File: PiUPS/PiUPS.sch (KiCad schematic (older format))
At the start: 93 parts, among them J1 USB_C_Receptacle_USB2.0, J2 Raspberry_Pi_2_3, J3 USB_A, J4 USB_B_Micro, J5 Screw_Terminal_01x02, J6 Screw_Terminal_01x02, Q1 IRF7404, Q2 IRF7404, Q3 IRLML2803TRPBF, Q4 IRF7404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

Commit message: Updated to include the boges to rev 0.2
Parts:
- removed C8: 100nF, Capacitor_SMD:C_0805_2012Metric_Pad1.18x1.45mm_HandSolder, symbol Device:C
- R14: value 470 -> 100
- R8: value 10k -> 1k
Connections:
- no-connect marks 33 -> 36
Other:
- note added: "(200k)\n\n"
- note added: "(62k)"
- note added: "Ports and outputs + RTC"
- note removed: "Ports and outputs"
- moved on the sheet: BT1, C1, C10, C11, C12, C13, C14, C15, C16, C17, C18, C19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

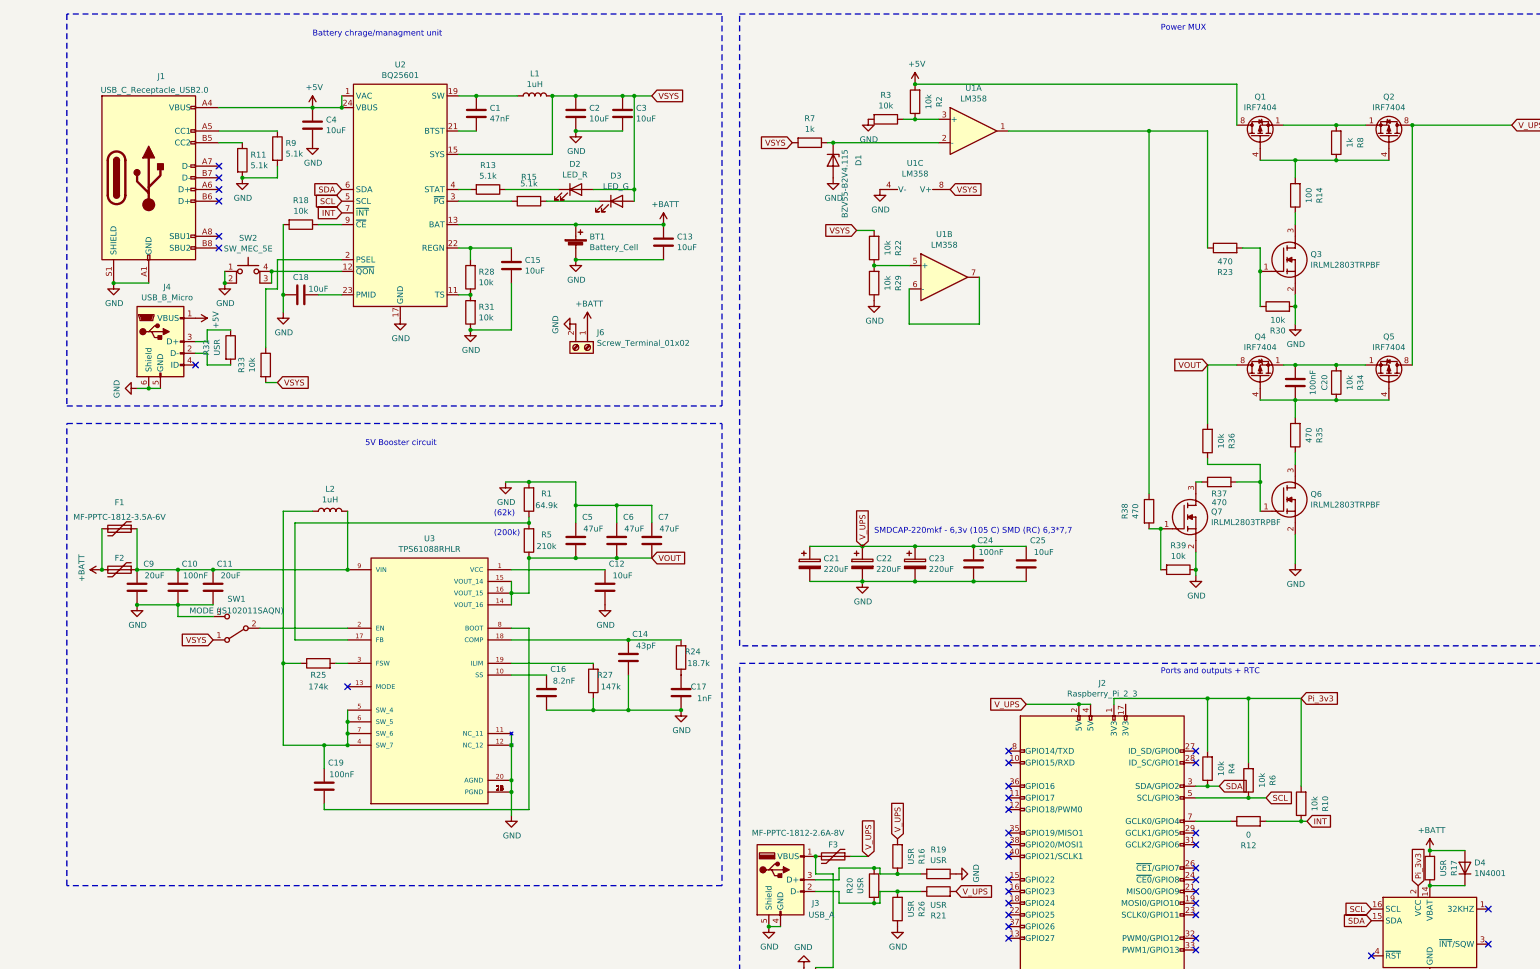
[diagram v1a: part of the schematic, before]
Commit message: added exprimental latching boost IC cutoff circuit + notes about dev branch file and future things to do
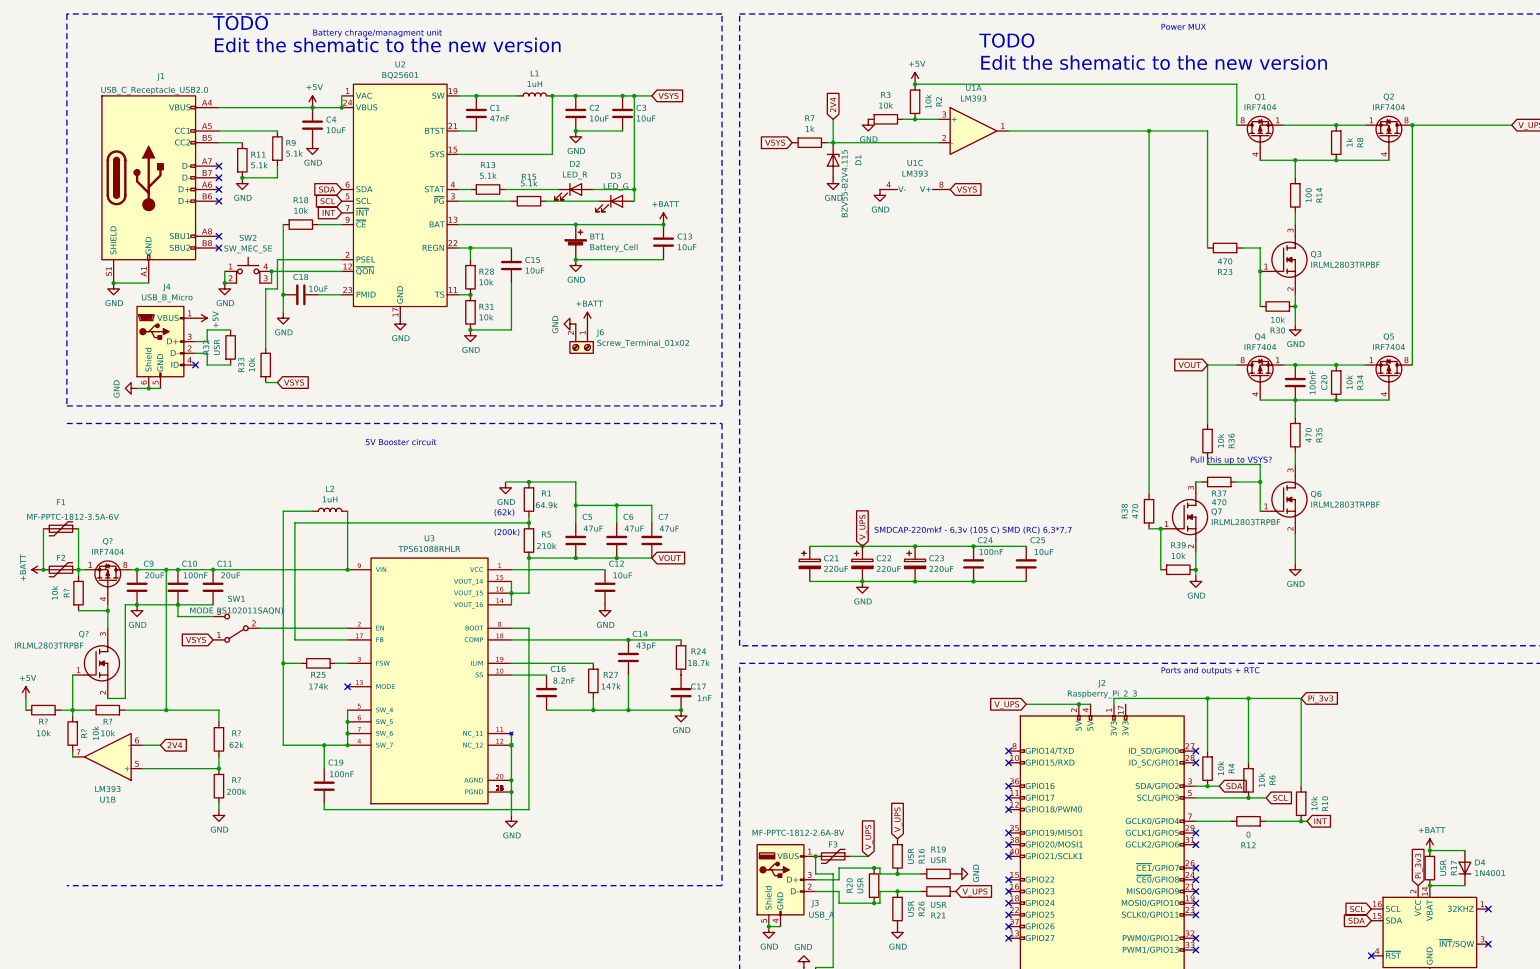
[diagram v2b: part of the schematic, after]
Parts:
- removed R22, R29: 10k, Resistor_SMD:R_0805_2012Metric_Pad1.20x1.40mm_HandSolder, symbol Device:R
- added Q?: IRF7404, Package_SO:SOIC-8_3.9x4.9mm_P1.27mm, symbol Transistor_FET:IRF7404
- added Q?: IRLML2803TRPBF, IRLML2803TRPBF:SOT95P237X112-3N, symbol IRLML2803TRPBF:IRLML2803TRPBF
- added R? (x4): 10k, Resistor_SMD:R_0805_2012Metric_Pad1.20x1.40mm_HandSolder, symbol Device:R
- added R?: 200k, Resistor_SMD:R_0805_2012Metric_Pad1.20x1.40mm_HandSolder, symbol Device:R
- added R?: 62k, Resistor_SMD:R_0805_2012Metric_Pad1.20x1.40mm_HandSolder, symbol Device:R
- U1: value LM358 -> LM393
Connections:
- net +5V: now also R?.1
- net GND: now also Q?.2, R?.1
- net at C10.1, C11.1, C9.1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: now also Q?.5 (D), Q?.6 (D), Q?.7 (D), Q?.8 (D), R?.2, R?.2; no longer F1.1, F2.1
- net 2V4: now reaches D1.1 (K), R7.1, U1.2 (-)
- net 2V4: now also U1.6 (-)
- net at U1.5 (+): now also R?.1, R?.2
- net at U1.7: now also R?.1; no longer U1.6 (-)
- new net: F1.1, F2.1, Q?.1 (S), Q?.2 (S), Q?.3 (S), R?.1
- new net: Q?.3, Q?.4 (G), R?.2
- new net: Q?.1, R?.1, R?.2, R?.2
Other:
- note added: "Pull this up to VSYS?"
- note added: "TODO\nEdit the shematic to the new version\n"
- moved on the sheet: F1, F2, U1B

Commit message: updated debug schematic
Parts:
- added C? (x2): 100nF, Capacitor_SMD:C_0805_2012Metric_Pad1.18x1.45mm_HandSolder, symbol Device:C
- added D?: 1N4007, Diode_THT:D_DO-41_SOD81_P10.16mm_Horizontal, symbol Diode:1N4007
- R14: value 100 -> 470
- R8: value 1k -> 10k
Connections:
- net +5V: now also D?.2 (A); no longer R?.1
- net GND: now also C?.2
- net at Q7.1, R38.2, R39.2: now also C?.1
- net at R2.1, R3.1, U1.3 (+): now also C?.2
- net at R?.1, R?.2, U1.5 (+): now also C?.1
- new net: D?.1 (K), R?.1
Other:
- moved on the sheet: U1C
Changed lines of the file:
@@
 L Amplifier_Operational:LM358 U1
 U 3 1 612A3B8B
-P 8450 2600
-F 0 "U1" V 8125 2600 50  0000 C CNN
-F 1 "LM393" V 8216 2600 50  0000 C CNN
-F 2 "Package_SO:SOIC-8_3.9x4.9mm_P1.27mm" H 8450 2600 50  0001 C CNN
-F 3 "http://www.ti.com/lit/ds/symlink/lm2904-n.pdf" H 8450 2600 50  0001 C CNN
-	3    8450 2600
+P 8200 3600
+F 0 "U1" V 7900 3400 50  0000 C CNN
+F 1 "LM393" V 8000 3400 50  0000 C CNN
+F 2 "Package_SO:SOIC-8_3.9x4.9mm_P1.27mm" H 8200 3600 50  0001 C CNN
+F 3 "http://www.ti.com/lit/ds/symlink/lm2904-n.pdf" H 8200 3600 50  0001 C CNN
+	3    8200 3600
 	0    1    1    0
 $EndComp
@@
 L power:GND #PWR010
 U 1 1 613779A5
-P 8150 2500
-F 0 "#PWR010" H 8150 2250 50  0001 C CNN
-F 1 "GND" H 8155 2327 50  0000 C CNN
-F 2 "" H 8150 2500 50  0001 C CNN
-F 3 "" H 8150 2500 50  0001 C CNN
-	1    8150 2500
-	1    0    0    -1
-$EndComp
-Text GLabel 8750 2500 2    50   Input ~ 0
+P 7900 3500
+F 0 "#PWR010" H 7900 3250 50  0001 C CNN
+F 1 "GND" H 7905 3327 50  0000 C CNN
+F 2 "" H 7900 3500 50  0001 C CNN
+F 3 "" H 7900 3500 50  0001 C CNN
+	1    7900 3500
+	1    0    0    -1
+$EndComp
+Text GLabel 8500 3500 2    50   Input ~ 0
 VSYS
 $Comp
@@
 P 12050 2100
 F 0 "R8" V 11843 2100 50  0000 C CNN
-F 1 "1k" V 11934 2100 50  0000 C CNN
+F 1 "10k" V 11934 2100 50  0000 C CNN
 F 2 "Resistor_SMD:R_0805_2012Metric_Pad1.20x1.40mm_HandSolder" V 11980 2100 50  0001 C CNN
 F 3 "~" H 12050 2100 50  0001 C CNN
@@
 P 11700 2550
 F 0 "R14" V 11493 2550 50  0000 C CNN
-F 1 "100" V 11584 2550 50  0000 C CNN
+F 1 "470" V 11584 2550 50  0000 C CNN
 F 2 "Resistor_SMD:R_0805_2012Metric_Pad1.20x1.40mm_HandSolder" V 11630 2550 50  0001 C CNN
 F 3 "~" H 11700 2550 50  0001 C CNN
@@
 L power:+5V #PWR?
 U 1 1 61994FA4
-P 850 6850
-F 0 "#PWR?" H 850 6700 50  0001 C CNN
-F 1 "+5V" H 865 7023 50  0000 C CNN
-F 2 "" H 850 6850 50  0001 C CNN
-F 3 "" H 850 6850 50  0001 C CNN
-	1    850  6850
+P 850 6550
+F 0 "#PWR?" H 850 6400 50  0001 C CNN
+F 1 "+5V" H 865 6723 50  0000 C CNN
+F 2 "" H 850 6550 50  0001 C CNN
+F 3 "" H 850 6550 50  0001 C CNN
+	1    850  6550
 	1    0    0    -1
 $EndComp
@@
 P 1250 6650
 F 0 "Q?" H 1300 7000 50  0000 L CNN
-F 1 "IRLML2803TRPBF" H 750 6900 50  0000 L CNN
+F 1 "IRLML2803TRPBF" H 800 7100 50  0000 L CNN
 F 2 "IRLML2803TRPBF:SOT95P237X112-3N" H 1700 6600 50  0001 L CNN
 F 3 "https://www.infineon.com/dgdl/irlml2803pbf.pdf?fileId=5546d462533600a4015356682aff260f" H 1700 6500 50  0001 L CNN
@@
 Text Notes 10800 4850 0    50   ~ 0
 Pull this up to VSYS?
+$Comp
+L Device:C C?
+U 1 1 6175D06B
+P 10300 5750
+F 0 "C?" H 10400 5950 50  0000 C CNN
+F 1 "100nF" H 10450 5850 50  0000 C CNN
+F 2 "Capacitor_SMD:C_0805_2012Metric_Pad1.18x1.45mm_HandSolder" H 10338 5600 50  0001 C CNN
+F 3 "~" H 10300 5750 50  0001 C CNN
+	1    10300 5750
+	1    0    0    -1
+$EndComp
+Wire Wire Line
+	10450 5400 10300 5400
+Wire Wire Line
+	10300 5400 10300 5600
+Connection ~ 10450 5400
+Wire Wire Line
+	10300 5900 10150 5900
+Wire Wire Line
+	10150 5900 10150 2800
+Wire Wire Line
+	10150 2800 8450 2800
+Wire Wire Line
+	8450 2800 8450 1900
+$Comp
+L Diode:1N4007 D?
+U 1 1 617EB5E7
+P 850 6700
+F 0 "D?" V 896 6620 50  0000 R CNN
+F 1 "1N4007" V 805 6620 50  0000 R CNN
+F 2 "Diode_THT:D_DO-41_SOD81_P10.16mm_Horizontal" H 850 6525 50  0001 C CNN
+F 3 "http://www.vishay.com/docs/88503/1n4001.pdf" H 850 6700 50  0001 C CNN
+	1    850  6700
+	0    -1   -1   0
+$EndComp
+$Comp
+L Device:C C?
+U 1 1 617F0600
+P 2950 7650
+F 0 "C?" H 3050 7850 50  0000 C CNN
+F 1 "100nF" H 3100 7750 50  0000 C CNN
+F 2 "Capacitor_SMD:C_0805_2012Metric_Pad1.18x1.45mm_HandSolder" H 2988 7500 50  0001 C CNN
+F 3 "~" H 2950 7650 50  0001 C CNN
+	1    2950 7650
+	1    0    0    -1
+$EndComp
+Wire Wire Line
+	2500 7450 2950 7450
+Wire Wire Line
+	2950 7450 2950 7500
+Wire Wire Line
+	2950 7800 2500 7800
+Connection ~ 2500 7800
 $EndSCHEMATC

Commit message: added almost final fixes for rev 0.1
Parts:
- removed C?: 100nF, Capacitor_SMD:C_0805_2012Metric_Pad1.18x1.45mm_HandSolder, symbol Device:C
- added R?: 100, Resistor_SMD:R_0805_2012Metric_Pad1.20x1.40mm_HandSolder, symbol Device:R
- C16: value 8.2nF -> 47nF
- D2: value LED_R -> LED_G
- D3: value LED_G -> LED_R
- R7: value 1k -> 470
- R?: value 62k -> 18k
- R? (x2): value 10k -> 470
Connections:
- net GND: no longer SW1.3 (C)
- net VOUT: now also SW1.2 (B)
- net VSYS: now also U3.2 (EN); no longer R7.2, SW1.1 (A), U1.8 (V+)
- net at R23.1, R38.1, U1.1: now also R?.1
- new net: R7.2, R?.2, SW1.1 (A), U1.8 (V+)
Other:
- note added: "(18k)\n"
- note added: "10uA leakage current at Vbat-2.5V"
- note added: "Probably can be lowered to 470"
- note added: "Suspected leakage current area?"
- moved on the sheet: SW1, U1C
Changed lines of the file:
@@
 P 5550 2500
 F 0 "D2" H 5543 2717 50  0000 C CNN
-F 1 "LED_R" H 5543 2626 50  0000 C CNN
+F 1 "LED_G" H 5543 2626 50  0000 C CNN
 F 2 "LED_SMD:LED_0805_2012Metric" H 5550 2500 50  0001 C CNN
 F 3 "~" H 5550 2500 50  0001 C CNN
@@
 P 5900 2600
 F 0 "D3" H 5893 2817 50  0000 C CNN
-F 1 "LED_G" H 5893 2726 50  0000 C CNN
+F 1 "LED_R" H 5893 2726 50  0000 C CNN
 F 2 "LED_SMD:LED_0805_2012Metric" H 5900 2600 50  0001 C CNN
 F 3 "~" H 5900 2600 50  0001 C CNN
@@
 P 5300 6800
 F 0 "C16" H 5400 7000 50  0000 C CNN
-F 1 "8.2nF" H 5450 6900 50  0000 C CNN
+F 1 "47nF" H 5450 6900 50  0000 C CNN
 F 2 "Capacitor_SMD:C_0805_2012Metric_Pad1.18x1.45mm_HandSolder" H 5338 6650 50  0001 C CNN
 F 3 "~" H 5300 6800 50  0001 C CNN
@@
 Wire Wire Line
 	6050 1700 6200 1700
-Text GLabel 2450 6350 0    50   Input ~ 0
-VSYS
 Wire Wire Line
 	2850 6250 3600 6250
-$Comp
-L Switch:SW_SPDT SW1
-U 1 1 612207C9
-P 2650 6250
-F 0 "SW1" H 2650 6000 50  0000 C CNN
-F 1 "MODE (JS102011SAQN)" H 2650 6100 50  0000 C CNN
-F 2 "Button_Switch_SMD:SW_SPDT_CK-JS102011SAQN" H 2650 6250 50  0001 C CNN
-F 3 "~" H 2650 6250 50  0001 C CNN
-	1    2650 6250
-	-1   0    0    1
-$EndComp
-Wire Wire Line
-	2450 6150 2150 6150
-Wire Wire Line
-	2150 6150 2150 6050
 Connection ~ 2150 6050
 Wire Notes Line
@@
 L Amplifier_Operational:LM358 U1
 U 3 1 612A3B8B
-P 8200 3600
-F 0 "U1" V 7900 3400 50  0000 C CNN
-F 1 "LM393" V 8000 3400 50  0000 C CNN
-F 2 "Package_SO:SOIC-8_3.9x4.9mm_P1.27mm" H 8200 3600 50  0001 C CNN
-F 3 "http://www.ti.com/lit/ds/symlink/lm2904-n.pdf" H 8200 3600 50  0001 C CNN
-	3    8200 3600
+P 8450 3250
+F 0 "U1" V 8150 3050 50  0000 C CNN
+F 1 "LM393" V 8250 3050 50  0000 C CNN
+F 2 "Package_SO:SOIC-8_3.9x4.9mm_P1.27mm" H 8450 3250 50  0001 C CNN
+F 3 "http://www.ti.com/lit/ds/symlink/lm2904-n.pdf" H 8450 3250 50  0001 C CNN
+	3    8450 3250
 	0    1    1    0
 $EndComp
@@
 	0    -1   -1   0
 $EndComp
-Text GLabel 7400 2100 0    50   Input ~ 0
-VSYS
 $Comp
 L power:GND #PWR09
@@
 P 7550 2100
 F 0 "R7" V 7343 2100 50  0000 C CNN
-F 1 "1k" V 7434 2100 50  0000 C CNN
+F 1 "470" V 7434 2100 50  0000 C CNN
 F 2 "Resistor_SMD:R_0805_2012Metric_Pad1.20x1.40mm_HandSolder" V 7480 2100 50  0001 C CNN
 F 3 "~" H 7550 2100 50  0001 C CNN
@@
 L power:GND #PWR010
 U 1 1 613779A5
-P 7900 3500
-F 0 "#PWR010" H 7900 3250 50  0001 C CNN
-F 1 "GND" H 7905 3327 50  0000 C CNN
-F 2 "" H 7900 3500 50  0001 C CNN
-F 3 "" H 7900 3500 50  0001 C CNN
-	1    7900 3500
-	1    0    0    -1
-$EndComp
-Text GLabel 8500 3500 2    50   Input ~ 0
-VSYS
+P 8150 3150
+F 0 "#PWR010" H 8150 2900 50  0001 C CNN
+F 1 "GND" H 8155 2977 50  0000 C CNN
+F 2 "" H 8150 3150 50  0001 C CNN
+F 3 "" H 8150 3150 50  0001 C CNN
+	1    8150 3150
+	1    0    0    -1
+$EndComp
 $Comp
 L Transistor_FET:IRF7404 Q2
@@
 Connection ~ 10550 5400
 Wire Wire Line
-	10450 5100 10450 2000
+	10450 5100 10450 2400
 Connection ~ 10450 2000
 Wire Wire Line
@@
 	-1   0    0    1
 $EndComp
-$Comp
-L Device:R R?
-U 1 1 6193474F
-P 2500 7200
-F 0 "R?" H 2350 7150 50  0000 C CNN
-F 1 "62k" H 2350 7250 50  0000 C CNN
-F 2 "Resistor_SMD:R_0805_2012Metric_Pad1.20x1.40mm_HandSolder" V 2430 7200 50  0001 C CNN
-F 3 "~" H 2500 7200 50  0001 C CNN
-	1    2500 7200
-	-1   0    0    1
-$EndComp
-Wire Wire Line
-	2500 7450 1850 7450
 Wire Wire Line
 	2500 7350 2500 7450
-Connection ~ 2500 7450
 $Comp
 L power:GND #PWR?
@@
 Wire Wire Line
 	2500 7800 2500 7750
-Wire Wire Line
-	2500 7050 2500 6950
-Wire Wire Line
-	2500 6950 2050 6950
 Connection ~ 2050 6950
 $Comp
@@
 P 1000 6950
 F 0 "R?" V 900 6950 50  0000 C CNN
-F 1 "10k" V 800 6950 50  0000 C CNN
+F 1 "470" V 800 6950 50  0000 C CNN
 F 2 "Resistor_SMD:R_0805_2012Metric_Pad1.20x1.40mm_HandSolder" V 930 6950 50  0001 C CNN
 F 3 "~" H 1000 6950 50  0001 C CNN
@@
 P 1250 7150
 F 0 "R?" V 1150 7150 50  0000 C CNN
-F 1 "10k" V 1050 7150 50  0000 C CNN
+F 1 "470" V 1050 7150 50  0000 C CNN
 F 2 "Resistor_SMD:R_0805_2012Metric_Pad1.20x1.40mm_HandSolder" V 1180 7150 50  0001 C CNN
 F 3 "~" H 1250 7150 50  0001 C CNN
@@
 	0    -1   -1   0
 $EndComp
-$Comp
-L Device:C C?
-U 1 1 617F0600
-P 2950 7650
-F 0 "C?" H 3050 7850 50  0000 C CNN
-F 1 "100nF" H 3100 7750 50  0000 C CNN
-F 2 "Capacitor_SMD:C_0805_2012Metric_Pad1.18x1.45mm_HandSolder" H 2988 7500 50  0001 C CNN
-F 3 "~" H 2950 7650 50  0001 C CNN
-	1    2950 7650
-	1    0    0    -1
-$EndComp
-Wire Wire Line
-	2500 7450 2950 7450
-Wire Wire Line
-	2950 7450 2950 7500
-Wire Wire Line
-	2950 7800 2500 7800
-Connection ~ 2500 7800
+Text GLabel 7400 3100 0    50   Input ~ 0
+VOUT
+$Comp
+L Device:R R?
+U 1 1 6189B0C4
+P 10300 2400
+F 0 "R?" V 10093 2400 50  0000 C CNN
+F 1 "100" V 10184 2400 50  0000 C CNN
+F 2 "Resistor_SMD:R_0805_2012Metric_Pad1.20x1.40mm_HandSolder" V 10230 2400 50  0001 C CNN
+F 3 "~" H 10300 2400 50  0001 C CNN
+	1    10300 2400
+	0    1    1    0
+$EndComp
+Connection ~ 10450 2400
+Wire Wire Line
+	10450 2400 10450 2000
+Text Notes 9950 2550 0    50   ~ 0
+Probably can be lowered to 470
+Text Notes 5700 3200 0    50   ~ 0
+10uA leakage current at Vbat-2.5V
+Wire Notes Line
+	650  5000 650  6150
+Wire Notes Line
+	650  6150 3300 6150
+Wire Notes Line
+	3300 6150 3300 5000
+Wire Notes Line
+	3300 5000 650  5000
+Text Notes 1550 5100 0    50   ~ 0
+Suspected leakage current area?
+Text Notes 6500 6350 0    50   ~ 0
+(18k)\n
+$Comp
+L Device:R R?
+U 1 1 6193474F
+P 2500 7200
+F 0 "R?" H 2350 7150 50  0000 C CNN
+F 1 "18k" H 2350 7250 50  0000 C CNN
+F 2 "Resistor_SMD:R_0805_2012Metric_Pad1.20x1.40mm_HandSolder" V 2430 7200 50  0001 C CNN
+F 3 "~" H 2500 7200 50  0001 C CNN
+	1    2500 7200
+	-1   0    0    1
+$EndComp
+Text GLabel 2850 6250 0    50   Input ~ 0
+VSYS
+$Comp
+L Switch:SW_SPDT SW1
+U 1 1 612207C9
+P 7600 3100
+F 0 "SW1" H 7600 2800 50  0000 C CNN
+F 1 "MODE (JS102011SAQN)" H 7450 2900 50  0000 C CNN
+F 2 "Button_Switch_SMD:SW_SPDT_CK-JS102011SAQN" H 7600 3100 50  0001 C CNN
+F 3 "~" H 7600 3100 50  0001 C CNN
+	1    7600 3100
+	1    0    0    -1
+$EndComp
+Wire Wire Line
+	2050 6950 2500 6950
+Wire Wire Line
+	2500 6950 2500 7050
+Wire Wire Line
+	1850 7450 2500 7450
+Connection ~ 2500 7450
+Wire Wire Line
+	7800 3000 8750 3000
+Wire Wire Line
+	8750 3000 8750 3150
+Wire Wire Line
+	7400 2100 7400 2900
+Wire Wire Line
+	7400 2900 7800 2900
+Wire Wire Line
+	7800 2900 7800 3000
+Connection ~ 7800 3000
+Wire Wire Line
+	10150 2400 9900 2400
+Wire Wire Line
+	9900 2400 9900 3000
+Wire Wire Line
+	9900 3000 8750 3000
+Connection ~ 8750 3000
 $EndSCHEMATC

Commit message: tidied up schematic
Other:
- note removed: "Suspected leakage current area?"
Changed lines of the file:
@@
 Connection ~ 2150 6050
 Wire Notes Line
-	1200 4500 6800 4500
-Wire Notes Line
 	6800 4500 6800 8450
-Wire Notes Line
-	6800 8450 1200 8450
 Text Notes 3750 4700 0    50   ~ 0
 5V Booster circuit
@@
 Text Notes 5700 3200 0    50   ~ 0
 10uA leakage current at Vbat-2.5V
-Wire Notes Line
-	650  5000 650  6150
-Wire Notes Line
-	650  6150 3300 6150
-Wire Notes Line
-	3300 6150 3300 5000
-Wire Notes Line
-	3300 5000 650  5000
-Text Notes 1550 5100 0    50   ~ 0
-Suspected leakage current area?
 Text Notes 6500 6350 0    50   ~ 0
 (18k)\n
@@
 	9900 3000 8750 3000
 Connection ~ 8750 3000
+Wire Notes Line
+	600  8450 600  4500
+Wire Notes Line
+	600  4500 6800 4500
+Wire Notes Line
+	600  8450 6800 8450
 $EndSCHEMATC
